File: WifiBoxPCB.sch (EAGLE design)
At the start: 4 parts, among them J1 CONNECTOR_PI_40_PIN, J2 microSD Socket, J3 OLED, U1 OLED_I2C

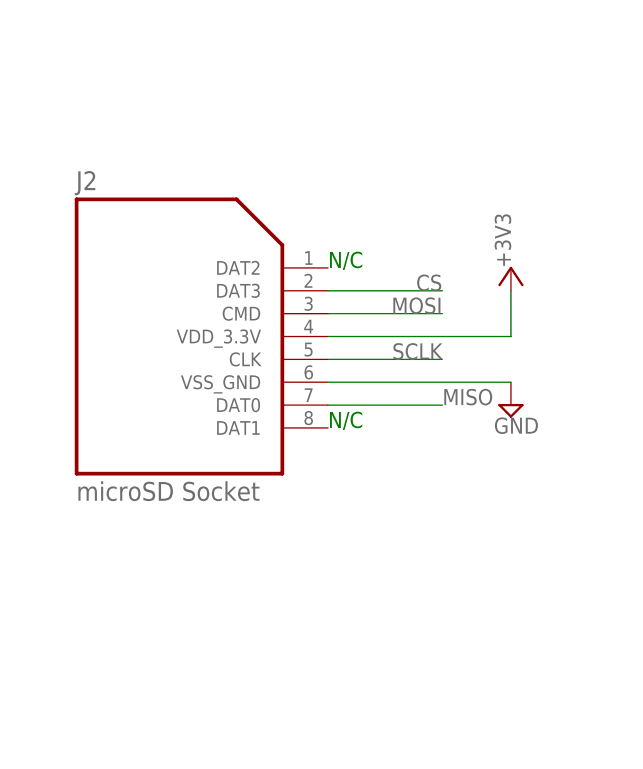
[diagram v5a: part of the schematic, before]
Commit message: updated rotation on the LED  also replaced SSD card socket to a push push holder
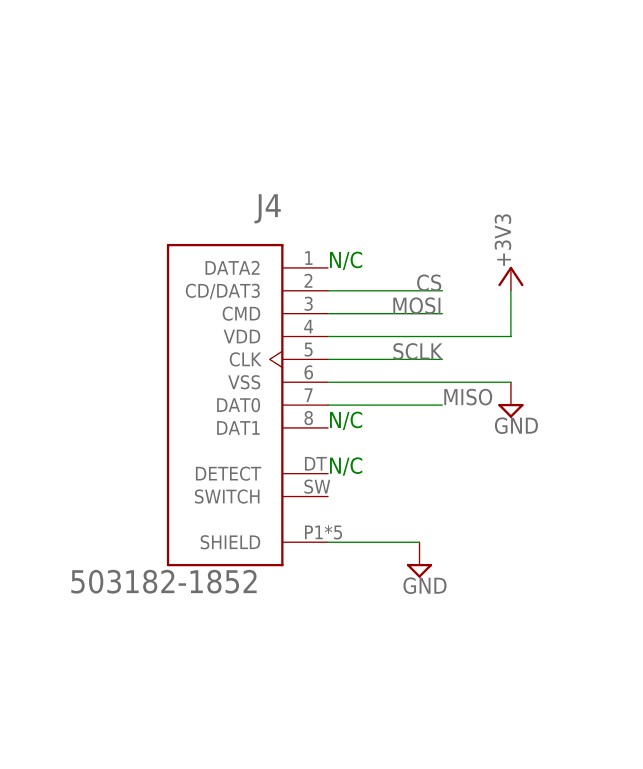
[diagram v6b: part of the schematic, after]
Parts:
- removed J2: microSD Socket, ConnectBox_2019:1140084168_1140084168
- added J4: 503182-1852, ConnectBox_2019:503182-1852
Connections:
- net +3V3: now also J4.VDD; no longer J2.VDD_3.3V@4
- net CS: now also J4.CD/DAT3; no longer J2.DAT3@2
- net GND: now also J4.SHIELD, J4.VSS; no longer J2.VSS_GND@6
- net MISO: now also J4.DAT0; no longer J2.DAT0@7
- net MOSI: now also J4.CMD; no longer J2.CMD@3
- net SCLK: now also J4.CLK; no longer J2.CLK@5
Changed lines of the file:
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@@
 <parts>
 <part name="FRAME1" library="ConnectBox_2019" deviceset="FRAMES_LETTER_L" device=""/>
-<part name="J2" library="ConnectBox_2019" deviceset="1140084168_1140084168" device="" value="microSD Socket"/>
 <part name="J1" library="ConnectBox_2019" deviceset="CONNECTOR_PI_40_PIN" device=""/>
 <part name="+3V1" library="ConnectBox_2019" deviceset="+3V3" device=""/>
@@
 <part name="SUPPLY3" library="ConnectBox_2019" deviceset="GND" device=""/>
 <part name="J3" library="ConnectBox_2019" deviceset="CONNECTOR_4" device="" value="OLED"/>
+<part name="J4" library="ConnectBox_2019" deviceset="503182-1852" device=""/>
+<part name="SUPPLY4" library="ConnectBox_2019" deviceset="GND" device=""/>
 </parts>
 <sheets>
@@
 <text x="76.2" y="114.3" size="1.778" layer="91">N/C</text>
 <text x="76.2" y="96.52" size="1.778" layer="91">N/C</text>
+<text x="76.2" y="91.44" size="1.778" layer="91">N/C</text>
 </plain>
 <instances>
@@
 <attribute name="SHEET" x="233.68" y="1.27" size="2.54" layer="94"/>
 <attribute name="DRAWING_NAME" x="165.1" y="19.05" size="2.54" layer="94"/>
-</instance>
-<instance part="J2" gate="G$1" x="60.96" y="104.14" smashed="yes">
-<attribute name="NAME" x="48.1914" y="122.94326875" size="2.08841875" layer="95" ratio="10" rot="SR0"/>
-<attribute name="VALUE" x="48.2307" y="88.4277" size="2.085209375" layer="96" ratio="10" rot="SR0"/>
 </instance>
 <instance part="J1" gate="G$1" x="147.32" y="101.6" smashed="yes">
@@
 <attribute name="NAME" x="218.44" y="129.54" size="2.0828" layer="95" rot="MR180" align="center"/>
 </instance>
+<instance part="J4" gate="G$1" x="71.12" y="99.06" smashed="yes" rot="MR0">
+<attribute name="NAME" x="71.12" y="119.9456" size="2.548" layer="95" rot="MR0"/>
+<attribute name="VALUE" x="68.58" y="78.165" size="2.548159375" layer="96" rot="MR0"/>
+</instance>
+<instance part="SUPPLY4" gate="GND" x="86.36" y="81.28" smashed="yes">
+<attribute name="VALUE" x="84.455" y="78.105" size="1.778" layer="96"/>
+</instance>
 </instances>
 <busses>
@@
 <net name="CS" class="0">
 <segment>
-<pinref part="J2" gate="G$1" pin="DAT3@2"/>
 <wire x1="88.9" y1="111.76" x2="76.2" y2="111.76" width="0.1524" layer="91"/>
 <label x="88.9" y="111.76" size="1.778" layer="95" rot="MR0"/>
+<pinref part="J4" gate="G$1" pin="CD/DAT3"/>
 </segment>
 <segment>
@@
 <net name="MOSI" class="0">
 <segment>
-<pinref part="J2" gate="G$1" pin="CMD@3"/>
 <wire x1="88.9" y1="109.22" x2="76.2" y2="109.22" width="0.1524" layer="91"/>
 <label x="88.9" y="109.22" size="1.778" layer="95" rot="MR0"/>
+<pinref part="J4" gate="G$1" pin="CMD"/>
 </segment>
 <segment>
@@
 </segment>
 <segment>
-<pinref part="J2" gate="G$1" pin="VDD_3.3V@4"/>
 <pinref part="+3V2" gate="G$1" pin="+3V3"/>
 <wire x1="96.52" y1="111.76" x2="96.52" y2="106.68" width="0.1524" layer="91"/>
 <wire x1="96.52" y1="106.68" x2="76.2" y2="106.68" width="0.1524" layer="91"/>
+<pinref part="J4" gate="G$1" pin="VDD"/>
 </segment>
 <segment>
@@
 <net name="GND" class="0">
 <segment>
-<pinref part="J2" gate="G$1" pin="VSS_GND@6"/>
 <pinref part="SUPPLY1" gate="GND" pin="GND"/>
 <wire x1="96.52" y1="101.6" x2="76.2" y2="101.6" width="0.1524" layer="91"/>
+<pinref part="J4" gate="G$1" pin="VSS"/>
 </segment>
 <segment>
@@
 <pinref part="J3" gate="G$1" pin="1"/>
 </segment>
+<segment>
+<pinref part="J4" gate="G$1" pin="SHIELD"/>
+<pinref part="SUPPLY4" gate="GND" pin="GND"/>
+<wire x1="86.36" y1="83.82" x2="76.2" y2="83.82" width="0.1524" layer="91"/>
+</segment>
 </net>
 <net name="SCLK" class="0">
 <segment>
-<pinref part="J2" gate="G$1" pin="CLK@5"/>
 <wire x1="88.9" y1="104.14" x2="76.2" y2="104.14" width="0.1524" layer="91"/>
 <label x="88.9" y="104.14" size="1.778" layer="95" rot="MR0"/>
+<pinref part="J4" gate="G$1" pin="CLK"/>
 </segment>
 <segment>
@@
 <net name="MISO" class="0">
 <segment>
-<pinref part="J2" gate="G$1" pin="DAT0@7"/>
 <wire x1="88.9" y1="99.06" x2="76.2" y2="99.06" width="0.1524" layer="91"/>
 <label x="88.9" y="99.06" size="1.778" layer="95"/>
+<pinref part="J4" gate="G$1" pin="DAT0"/>
 </segment>
 <segment>

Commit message: 3rd round of updates removing the OLED
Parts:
- J1: value CONNECTOR_PI_40_PIN -> CONNECTOR_PI_24_PIN; device ConnectBox_2019:CONNECTOR_PI_40_PIN -> ConnectBox_2019:CONNECTOR_PI_24_PIN
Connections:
- removed net SCK: J1.I2C_SCL@5, J3.3
- removed net SDA: J1.I2C_SDA@3, J3.4
- net +3V3: no longer J3.2
- net GND: now also J1.GND@9; no longer J1.GND@39, J3.1
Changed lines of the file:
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@@
 <parts>
 <part name="FRAME1" library="ConnectBox_2019" deviceset="FRAMES_LETTER_L" device=""/>
-<part name="J1" library="ConnectBox_2019" deviceset="CONNECTOR_PI_40_PIN" device=""/>
+<part name="J1" library="ConnectBox_2019" deviceset="CONNECTOR_PI_24_PIN" device=""/>
 <part name="+3V1" library="ConnectBox_2019" deviceset="+3V3" device=""/>
 <part name="+3V2" library="ConnectBox_2019" deviceset="+3V3" device=""/>
@@
 <segment>
 <pinref part="J1" gate="G$1" pin="SPI_CE0@24"/>
-<wire x1="182.88" y1="93.98" x2="170.18" y2="93.98" width="0.1524" layer="91"/>
-<label x="182.88" y="93.98" size="1.778" layer="95" rot="MR0"/>
+<wire x1="170.18" y1="91.44" x2="177.8" y2="91.44" width="0.1524" layer="91"/>
+<label x="177.8" y="91.44" size="1.778" layer="95"/>
 </segment>
 </net>
@@
 <segment>
 <pinref part="J1" gate="G$1" pin="SPI_MOSI@19"/>
-<wire x1="111.76" y1="104.14" x2="124.46" y2="104.14" width="0.1524" layer="91"/>
-<label x="111.76" y="104.14" size="1.778" layer="95"/>
+<wire x1="124.46" y1="101.6" x2="116.84" y2="101.6" width="0.1524" layer="91"/>
+<label x="111.76" y="101.6" size="1.778" layer="95"/>
 </segment>
 </net>
 <net name="+3V3" class="0">
-<segment>
-<pinref part="J1" gate="G$1" pin="3.3V@1"/>
-<pinref part="+3V1" gate="G$1" pin="+3V3"/>
-<wire x1="114.3" y1="154.94" x2="114.3" y2="149.86" width="0.1524" layer="91"/>
-<wire x1="114.3" y1="149.86" x2="124.46" y2="149.86" width="0.1524" layer="91"/>
-</segment>
 <segment>
 <pinref part="+3V2" gate="G$1" pin="+3V3"/>
@@
 </segment>
 <segment>
-<pinref part="+3V3" gate="G$1" pin="+3V3"/>
-<wire x1="193.04" y1="121.92" x2="208.28" y2="121.92" width="0.1524" layer="91"/>
-<pinref part="J3" gate="G$1" pin="2"/>
+<pinref part="J1" gate="G$1" pin="3.3V@1"/>
+<wire x1="124.46" y1="147.32" x2="119.38" y2="147.32" width="0.1524" layer="91"/>
+<label x="114.3" y="147.32" size="1.778" layer="95"/>
 </segment>
 </net>
@@
 </segment>
 <segment>
-<pinref part="J1" gate="G$1" pin="GND@39"/>
-<pinref part="SUPPLY2" gate="GND" pin="GND"/>
-<wire x1="114.3" y1="53.34" x2="124.46" y2="53.34" width="0.1524" layer="91"/>
-</segment>
-<segment>
-<pinref part="SUPPLY3" gate="GND" pin="GND"/>
-<wire x1="200.66" y1="134.62" x2="208.28" y2="134.62" width="0.1524" layer="91"/>
-<wire x1="208.28" y1="134.62" x2="208.28" y2="124.46" width="0.1524" layer="91"/>
-<pinref part="J3" gate="G$1" pin="1"/>
-</segment>
-<segment>
 <pinref part="J4" gate="G$1" pin="SHIELD"/>
 <pinref part="SUPPLY4" gate="GND" pin="GND"/>
 <wire x1="86.36" y1="83.82" x2="76.2" y2="83.82" width="0.1524" layer="91"/>
+</segment>
+<segment>
+<pinref part="J1" gate="G$1" pin="GND@9"/>
+<wire x1="124.46" y1="127" x2="119.38" y2="127" width="0.1524" layer="91"/>
+<label x="114.3" y="127" size="1.778" layer="95"/>
 </segment>
 </net>
@@
 <segment>
 <pinref part="J1" gate="G$1" pin="SPI_SCLK@23"/>
-<wire x1="111.76" y1="93.98" x2="124.46" y2="93.98" width="0.1524" layer="91"/>
-<label x="111.76" y="93.98" size="1.778" layer="95"/>
+<wire x1="124.46" y1="91.44" x2="116.84" y2="91.44" width="0.1524" layer="91"/>
+<label x="111.76" y="91.44" size="1.778" layer="95"/>
 </segment>
 </net>
@@
 <segment>
 <pinref part="J1" gate="G$1" pin="SPI_MISO@21"/>
-<wire x1="111.76" y1="99.06" x2="124.46" y2="99.06" width="0.1524" layer="91"/>
-<label x="111.76" y="99.06" size="1.778" layer="95"/>
-</segment>
-</net>
-<net name="SCK" class="0">
-<segment>
-<wire x1="208.28" y1="119.38" x2="198.12" y2="119.38" width="0.1524" layer="91"/>
-<label x="198.12" y="119.38" size="1.778" layer="95"/>
-<pinref part="J3" gate="G$1" pin="3"/>
-</segment>
-<segment>
-<pinref part="J1" gate="G$1" pin="I2C_SCL@5"/>
-<wire x1="124.46" y1="139.7" x2="114.3" y2="139.7" width="0.1524" layer="91"/>
-<label x="114.3" y="139.7" size="1.778" layer="95"/>
-</segment>
-</net>
-<net name="SDA" class="0">
-<segment>
-<wire x1="208.28" y1="116.84" x2="198.12" y2="116.84" width="0.1524" layer="91"/>
-<label x="198.12" y="116.84" size="1.778" layer="95"/>
-<pinref part="J3" gate="G$1" pin="4"/>
-</segment>
-<segment>
-<pinref part="J1" gate="G$1" pin="I2C_SDA@3"/>
-<wire x1="114.3" y1="144.78" x2="124.46" y2="144.78" width="0.1524" layer="91"/>
-<label x="114.3" y="144.78" size="1.778" layer="95"/>
+<wire x1="124.46" y1="96.52" x2="116.84" y2="96.52" width="0.1524" layer="91"/>
+<label x="111.76" y="96.52" size="1.778" layer="95"/>
 </segment>
 </net>
@@
 </schematic>
 </drawing>
-<compatibility>
-<note version="8.3" severity="warning">
-Since Version 8.3, EAGLE supports URNs for individual library
-assets (packages, symbols, and devices). The URNs of those assets
-will not be understood (or retained) with this version.
-</note>
-</compatibility>
 </eagle>
